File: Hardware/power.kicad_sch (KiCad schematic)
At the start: 21 parts, among them U3 LM66200DRLR, U4 MAX77827AEFD+T, U5 SC4215

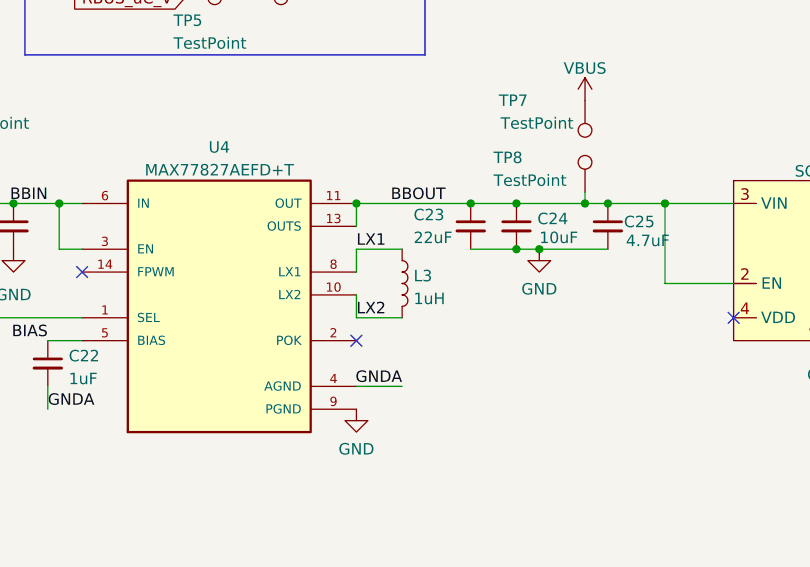
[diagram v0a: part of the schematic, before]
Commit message: on the verge of being complete, also updated to kicad 7
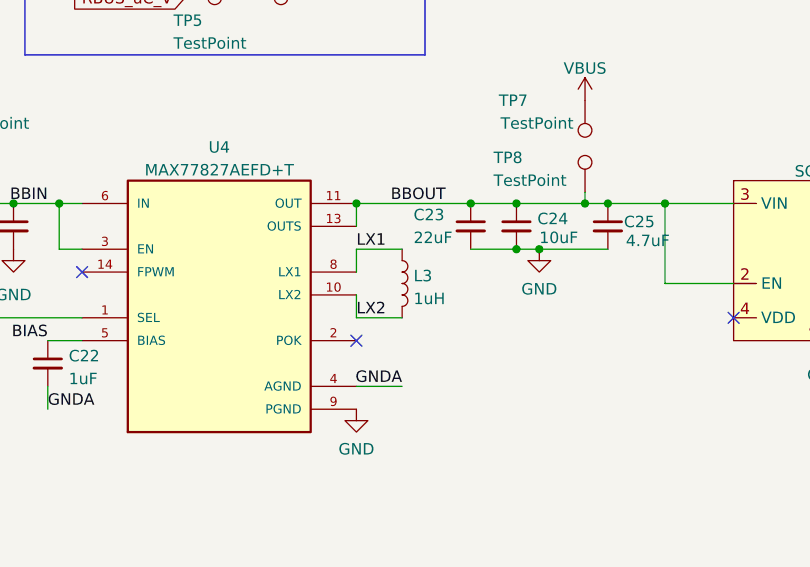
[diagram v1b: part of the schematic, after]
